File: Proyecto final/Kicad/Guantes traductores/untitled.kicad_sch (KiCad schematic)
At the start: 1 part, among them U6 TPS63020

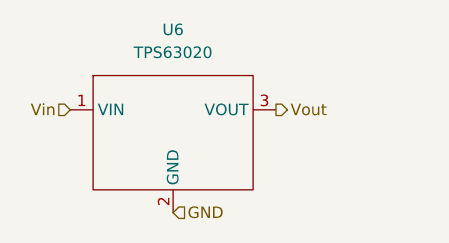
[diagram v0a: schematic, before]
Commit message: Posicion de componentes
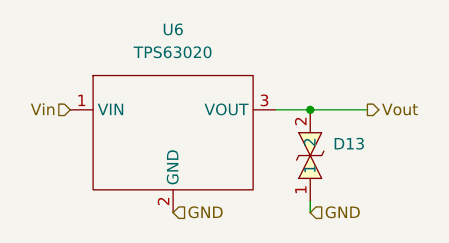
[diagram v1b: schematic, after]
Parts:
- added D13: ESD5B5.0ST1G, Diode_SMD:D_SOD-523, symbol ESD5B5.0ST1G:ESD5B5.0ST1G
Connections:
- net GND: now also D13.1
- net Vout: now also D13.2
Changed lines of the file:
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@@
 (kicad_sch
-	(version 20250114)
+	(version 20260306)
 	(generator "eeschema")
-	(generator_version "9.0")
+	(generator_version "10.0")
 	(paper "A4")
+	(junction
+		(at 116.84 63.5)
+		(diameter 0)
+		(color 0 0 0 0)
+	)
+	(wire
+		(pts
+			(xy 123.19 63.5) (xy 116.84 63.5)
+		)
+		(stroke
+			(width 0)
+			(type default)
+		)
+	)
+	(wire
+		(pts
+			(xy 116.84 63.5) (xy 113.03 63.5)
+		)
+		(stroke
+			(width 0)
+			(type default)
+		)
+	)
+	(wire
+		(pts
+			(xy 116.84 73.66) (xy 116.84 74.93)
+		)
+		(stroke
+			(width 0)
+			(type default)
+		)
+	)
+	(hierarchical_label "GND"
+		(shape input)
+		(at 116.84 74.93 0)
+		(effects
+			(font
+				(size 1.27 1.27)
+			)
+			(justify left)
+		)
+	)
 	(hierarchical_label "Vout"
 		(shape output)
-		(at 113.03 63.5 0)
+		(at 123.19 63.5 0)
 		(effects
 			(font
@@
 			)
 			(justify left)
+		)
+	)
+	(symbol
+		(lib_id "ESD5B5.0ST1G:ESD5B5.0ST1G")
+		(at 116.84 68.58 90)
+		(unit 1)
+		(body_style 1)
+		(exclude_from_sim no)
+		(in_bom yes)
+		(on_board yes)
+		(in_pos_files yes)
+		(dnp no)
+		(property "Reference" "D13"
+			(at 119.38 67.3099 90)
+			(show_name no)
+			(do_not_autoplace no)
+			(effects
+				(font
+					(size 1.27 1.27)
+				)
+				(justify right)
+			)
+		)
+		(property "Value" "ESD5B5.0ST1G"
+			(at 118.11 61.214 90)
+			(hide yes)
+			(show_name no)
+			(do_not_autoplace no)
+			(effects
+				(font
+					(size 1.27 1.27)
+				)
+				(justify right)
+			)
+		)
+		(property "Footprint" "Diode_SMD:D_SOD-523"
+			(at 124.46 68.58 0)
+			(hide yes)
+			(show_name no)
+			(do_not_autoplace no)
+			(effects
+				(font
+					(size 1.27 1.27)
+				)
+			)
+		)
+		(property "Datasheet" "https://lcsc.com/product-detail/Diodes-ESD_ON_ESD5B5-0ST1G_ESD5B5-0ST1G_C93623.html"
+			(at 127 68.58 0)
+			(hide yes)
+			(show_name no)
+			(do_not_autoplace no)
+			(effects
+				(font
+					(size 1.27 1.27)
+				)
+			)
+		)
+		(property "Description" ""
+			(at 116.84 68.58 0)
+			(hide yes)
+			(show_name no)
+			(do_not_autoplace no)
+			(effects
+				(font
+					(size 1.27 1.27)
+				)
+			)
+		)
+		(property "Manufacturer" "onsemi(安森美)"
+			(at 129.54 68.58 0)
+			(hide yes)
+			(show_name no)
+			(do_not_autoplace no)
+			(effects
+				(font
+					(size 1.27 1.27)
+				)
+			)
+		)
+		(property "MPN" "ESD5B5.0ST1G"
+			(at 132.08 68.58 0)
+			(hide yes)
+			(show_name no)
+			(do_not_autoplace no)
+			(effects
+				(font
+					(size 1.27 1.27)
+				)
+			)
+		)
+		(property "LCSC Part" "C93623"
+			(at 134.62 68.58 0)
+			(hide yes)
+			(show_name no)
+			(do_not_autoplace no)
+			(effects
+				(font
+					(size 1.27 1.27)
+				)
+			)
+		)
+		(pin "2"
+		)
+		(pin "1"
+		)
+		(instances
+			(project "Guantes traductores"
+				(path "/00699b90-32f8-49a9-88ac-8ba611fc0511/b987569c-50a5-4036-be29-da17e945f358"
+					(reference "D13")
+					(unit 1)
+				)
+			)
 		)
 	)
@@
 		(at 92.71 59.69 0)
 		(unit 1)
+		(body_style 1)
 		(exclude_from_sim no)
 		(in_bom yes)
 		(on_board yes)
+		(in_pos_files yes)
 		(dnp no)
 		(fields_autoplaced yes)
 		(property "Reference" "U6"
 			(at 101.6 54.61 0)
+			(show_name no)
+			(do_not_autoplace no)
 			(effects
 				(font
@@
 		(property "Value" "TPS63020"
 			(at 101.6 57.15 0)
+			(show_name no)
+			(do_not_autoplace no)
 			(effects
 				(font
@@
 		(property "Footprint" "Custom board:TPS63020 Board"
 			(at 92.71 59.69 0)
-			(effects
-				(font
-					(size 1.27 1.27)
-				)
-				(hide yes)
+			(hide yes)
+			(show_name no)
+			(do_not_autoplace no)
+			(effects
+				(font
+					(size 1.27 1.27)
+				)
 			)
 		)
 		(property "Datasheet" ""
 			(at 92.71 59.69 0)
-			(effects
-				(font
-					(size 1.27 1.27)
-				)
-				(hide yes)
+			(hide yes)
+			(show_name no)
+			(do_not_autoplace no)
+			(effects
+				(font
+					(size 1.27 1.27)
+				)
 			)
 		)
 		(property "Description" "Buck/boost, 2-5.5V IN, 3.3-5V OUT"
 			(at 103.632 55.88 0)
-			(effects
-				(font
-					(size 1.27 1.27)
-				)
-				(hide yes)
-			)
-		)
+			(hide yes)
+			(show_name no)
+			(do_not_autoplace no)
+			(effects
+				(font
+					(size 1.27 1.27)
+				)
+			)
+		)

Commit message: Enrutado TPS63020
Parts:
- removed U6: TPS63020, Custom board:TPS63020 Board, symbol Custom board:TPS63020
- added C16, C17: 10uf, Capacitor_SMD:C_0805_2012Metric_Pad1.18x1.45mm_HandSolder, symbol Device:C
- added C18: 100nf, Capacitor_SMD:C_0805_2012Metric_Pad1.18x1.45mm_HandSolder, symbol Device:C
- added C19, C20, C21: 22uf, Capacitor_SMD:C_0805_2012Metric_Pad1.18x1.45mm_HandSolder, symbol Device:C
- added L1: 1.5uH, L_APV_APH0630, symbol Device:L
- added R23, R26: 1M, Resistor_SMD:R_0805_2012Metric_Pad1.20x1.40mm_HandSolder, symbol Device:R
- added R25: 180K, Resistor_SMD:R_0805_2012Metric_Pad1.20x1.40mm_HandSolder, symbol Device:R
- added U10: TPS63020DSJR, Custom board:IC_TPS63020DSJR, symbol TPS63020DSJR:TPS63020DSJR
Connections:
- net GND: now also C16.2, C17.2, C18.2, C19.2, C20.2, C21.2, R25.2, U10.13 (PS/SYNC), U10.15 (PGND), U10.2 (GND)
- net Vin: now also C16.1, C17.1, C18.1, U10.1 (VINA), U10.10 (VIN_10), U10.11 (VIN_11), U10.12 (EN)
- net Vout: now also C19.1, C20.1, C21.1, R23.1, R26.1, U10.4 (VOUT_4), U10.5 (VOUT_5)
- new net: L1.1, U10.8 (L1_8), U10.9 (L1_9)
- new net: L1.2, U10.6 (L2_6), U10.7 (L2_7)
- new net: R26.2, U10.14 (PG)
- new net: R23.2, R25.1, U10.3 (FB)

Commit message: Ajustes vias de esp32
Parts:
- added J2: Conn_01x03_Pin, Connector_PinHeader_2.54mm:PinHeader_1x03_P2.54mm_Vertical, symbol Connector:Conn_01x03_Pin
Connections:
- net GND: now also J2.2 (Pin_2)
- net Vin: now also J2.1 (Pin_1)
- net Vout: now also J2.3 (Pin_3)
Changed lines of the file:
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@@
+	(wire
+		(pts
+			(xy 158.75 58.42) (xy 158.75 59.69)
+		)
+		(stroke
+			(width 0)
+			(type default)
+		)
+	)
 	(wire
 		(pts
@@
 	(wire
 		(pts
+			(xy 149.86 58.42) (xy 158.75 58.42)
+		)
+		(stroke
+			(width 0)
+			(type default)
+		)
+	)
+	(wire
+		(pts
 			(xy 143.51 128.27) (xy 143.51 132.08)
 		)
@@
 			(width 0)
 			(type default)
+		)
+	)
+	(hierarchical_label "Vin"
+		(shape input)
+		(at 149.86 55.88 0)
+		(effects
+			(font
+				(size 1.27 1.27)
+			)
+			(justify left)
 		)
 	)
@@
 			)
 			(justify right)
+		)
+	)
+	(hierarchical_label "Vout"
+		(shape output)
+		(at 149.86 60.96 0)
+		(effects
+			(font
+				(size 1.27 1.27)
+			)
+			(justify left)
 		)
 	)
@@
 	)
 	(symbol
+		(lib_id "power:GND")
+		(at 158.75 59.69 0)
+		(unit 1)
+		(body_style 1)
+		(exclude_from_sim no)
+		(in_bom yes)
+		(on_board yes)
+		(in_pos_files yes)
+		(dnp no)
+		(fields_autoplaced yes)
+		(property "Reference" "#PWR023"
+			(at 158.75 66.04 0)
+			(hide yes)
+			(show_name no)
+			(do_not_autoplace no)
+			(effects
+				(font
+					(size 1.27 1.27)
+				)
+			)
+		)
+		(property "Value" "GND"
+			(at 158.75 64.77 0)
+			(show_name no)
+			(do_not_autoplace no)
+			(effects
+				(font
+					(size 1.27 1.27)
+				)
+			)
+		)
+		(property "Footprint" ""
+			(at 158.75 59.69 0)
+			(hide yes)
+			(show_name no)
+			(do_not_autoplace no)
+			(effects
+				(font
+					(size 1.27 1.27)
+				)
+			)
+		)
+		(property "Datasheet" ""
+			(at 158.75 59.69 0)
+			(hide yes)
+			(show_name no)
+			(do_not_autoplace no)
+			(effects
+				(font
+					(size 1.27 1.27)
+				)
+			)
+		)
+		(property "Description" "Power symbol creates a global label with name \"GND\" , ground"
+			(at 158.75 59.69 0)
+			(hide yes)
+			(show_name no)
+			(do_not_autoplace no)
+			(effects
+				(font
+					(size 1.27 1.27)
+				)
+			)
+		)
+		(pin "1"
+		)
+		(instances
+			(project "Guantes traductores"
+				(path "/00699b90-32f8-49a9-88ac-8ba611fc0511/b987569c-50a5-4036-be29-da17e945f358"
+					(reference "#PWR023")
+					(unit 1)
+				)
+			)
+		)
+	)
+	(symbol
 		(lib_id "Device:C")
 		(at 93.98 111.76 0)
@@
 					(unit 1)
 				)
+			)
+		)
+	)
+	(symbol
+		(lib_id "Connector:Conn_01x03_Pin")
+		(at 144.78 58.42 0)
+		(unit 1)
+		(body_style 1)
+		(exclude_from_sim no)
+		(in_bom yes)
+		(on_board yes)
+		(in_pos_files yes)
+		(dnp no)
+		(fields_autoplaced yes)
+		(property "Reference" "J2"
+			(at 145.415 50.8 0)
+			(show_name no)
+			(do_not_autoplace no)
+			(effects
+				(font
+					(size 1.27 1.27)
+				)
+			)
+		)
+		(property "Value" "Conn_01x03_Pin"
+			(at 145.415 53.34 0)
+			(show_name no)
+			(do_not_autoplace no)
+			(effects
+				(font
+					(size 1.27 1.27)
+				)
+			)
+		)
+		(property "Footprint" "Connector_PinHeader_2.54mm:PinHeader_1x03_P2.54mm_Vertical"
+			(at 144.78 58.42 0)
+			(hide yes)
+			(show_name no)
+			(do_not_autoplace no)
+			(effects
+				(font
+					(size 1.27 1.27)
+				)
+			)
+		)
+		(property "Datasheet" ""
+			(at 144.78 58.42 0)
+			(hide yes)
+			(show_name no)
+			(do_not_autoplace no)
+			(effects
+				(font
+					(size 1.27 1.27)
+				)
+			)
+		)
+		(property "Description" "Generic connector, single row, 01x03, script generated"
+			(at 144.78 58.42 0)
+			(hide yes)
+			(show_name no)
+			(do_not_autoplace no)
+			(effects
+				(font
+					(size 1.27 1.27)
+				)
+			)
+		)
+		(pin "3"
+		)
+		(pin "2"
+		)
+		(pin "1"
+		)
+		(instances
+			(project "Guantes traductores"
+				(path "/00699b90-32f8-49a9-88ac-8ba611fc0511/b987569c-50a5-4036-be29-da17e945f358"
+					(reference "J2")
+					(unit 1)
+				)
